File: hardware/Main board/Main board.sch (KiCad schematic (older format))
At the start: 101 parts, among them J1 Wind Direction, J10 Free Pins, J11 Nokia 5110 LCD, J2 Wind Speed, J3 USB_B_Micro, J4 Micro_SD_Card, J5 Sensor board connector, J6 Barrel_Jack, J7 ISP programmer, J8 SPI1, J9 SPI2, Q1 IRLML2060, SW1 SW_Push, SW2 SW_SPST, SW3 SW_Push, SW4 SW_Push, SW5 Page Switch btn, U1 FT232RL, U2 MCP6042, U3 SCWN03A-03, U4 ATmega1284P-AU, U5 DS3231MZ, U6 ENC28J60, U7 USB6B1, U8 DRV5053, Y1 16MHZ

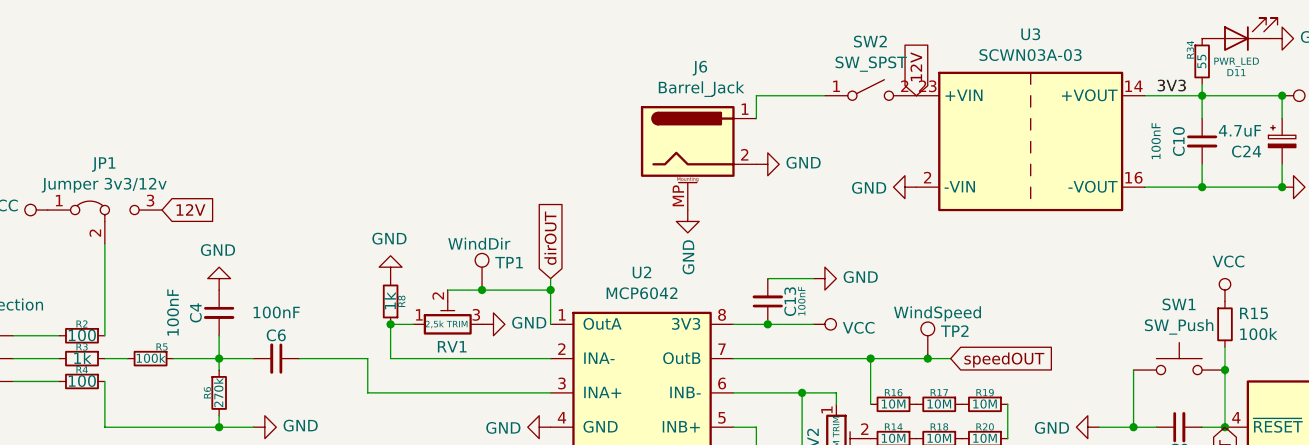
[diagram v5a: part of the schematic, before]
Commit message: Added protection for power input
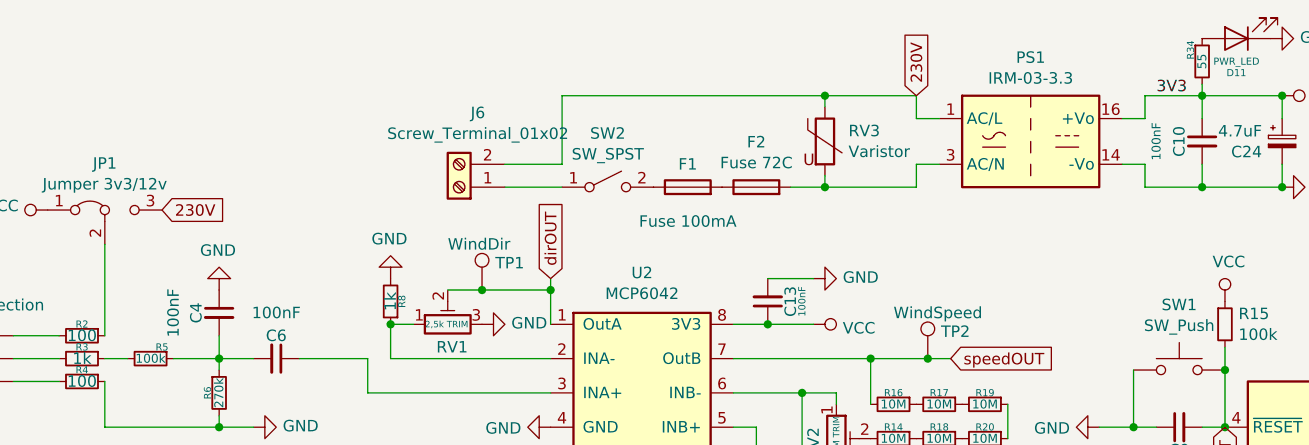
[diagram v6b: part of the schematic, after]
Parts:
- removed J6: Barrel_Jack, Connector_BarrelJack:BarrelJack_Horizontal, symbol Connector:Barrel_Jack_MountingPin
- removed U3: SCWN03A-03, Meteo_Footprints:SCWN03A, symbol Main-board-rescue:SCWN03A-03-Meteo_Station
- added F1: Fuse 100mA, Fuse:Fuseholder_Cylinder-5x20mm_Schurter_0031_8201_Horizontal_Open, symbol Device:Fuse
- added F2: Fuse 72C, Meteo_Footprints:Thermal fuse, symbol Device:Fuse
- added J6: Screw_Terminal_01x02, TerminalBlock_RND:TerminalBlock_RND_205-00298_1x02_P10.00mm_Horizontal, symbol Connector:Screw_Terminal_01x02
- added PS1: IRM-03-3.3, Converter_ACDC:Converter_ACDC_MeanWell_IRM-03-xx_THT, symbol Converter_ACDC:IRM-03-12
- added RV3: Varistor, Capacitor_SMD:C_0603_1608Metric_Pad1.05x0.95mm_HandSolder, symbol Device:Varistor
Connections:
- net GND: now also PS1.14 (-Vo)
- net VCC: now also PS1.16 (+Vo)
- net at SW2.1 (A): now also J6.1 (Pin_1)
- net 12V: no longer names the net of SW2.2 (B)
- net 12V: now also F1.1; no longer JP1.3 (B)
- new net: F1.2, F2.1
- new net: F2.2, PS1.3 (AC/N), RV3.2
- new net 230V: J6.2 (Pin_2), JP1.3 (B), PS1.1 (AC/L), RV3.1
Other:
- moved on the sheet: SW2
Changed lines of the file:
@@
 Wire Wire Line
 	2650 3450 3300 3450
-$Comp
-L Main-board-rescue:SCWN03A-03-Meteo_Station U3
-U 1 1 5D3F6E91
-P 5500 1000
-F 0 "U3" H 5500 1467 50  0000 C CNN
-F 1 "SCWN03A-03" H 5500 1376 50  0000 C CNN
-F 2 "Meteo_Footprints:SCWN03A" H 5500 650 50  0001 C CIN
-F 3 "" H 5500 550 50  0001 C CNN
-	1    5500 1000
-	1    0    0    -1
-$EndComp
 Wire Wire Line
 	6000 800  6250 800
@@
 NoConn ~ 9900 900
 $Comp
-L Connector:Barrel_Jack_MountingPin J6
-U 1 1 5D473214
-P 4000 1000
-F 0 "J6" H 4057 1325 50  0000 C CNN
-F 1 "Barrel_Jack" H 4057 1234 50  0000 C CNN
-F 2 "Connector_BarrelJack:BarrelJack_Horizontal" H 4050 960 50  0001 C CNN
-F 3 "~" H 4050 960 50  0001 C CNN
-	1    4000 1000
-	1    0    0    -1
-$EndComp
-$Comp
 L Device:R_Small R21
 U 1 1 5D4A50CE
@@
 L Switch:SW_SPST SW2
 U 1 1 5D4E4AA2
-P 4800 800
-F 0 "SW2" H 4800 1035 50  0000 C CNN
-F 1 "SW_SPST" H 4800 944 50  0000 C CNN
-F 2 "Meteo footprint:Switch_ON_OFF" H 4800 800 50  0001 C CNN
-F 3 "~" H 4800 800 50  0001 C CNN
-	1    4800 800
-	1    0    0    -1
-$EndComp
-Wire Wire Line
-	4300 900  4300 800
-Wire Wire Line
-	4300 800  4600 800
+P 3650 1200
+F 0 "SW2" H 3650 1435 50  0000 C CNN
+F 1 "SW_SPST" H 3650 1344 50  0000 C CNN
+F 2 "Meteo footprint:Switch_ON_OFF" H 3650 1200 50  0001 C CNN
+F 3 "~" H 3650 1200 50  0001 C CNN
+	1    3650 1200
+	1    0    0    -1
+$EndComp
 $Comp
 L Power_Protection:USB6B1 U7
@@
 $EndComp
 Text GLabel 5000 800  1    50   Input ~ 0
-12V
+230V
 Text GLabel 1700 1300 2    50   Input ~ 0
-12V
+230V
 Wire Wire Line
 	1450 1450 1450 1850
@@
 	6250 800  6250 750
 $Comp
-L power:GND #PWR0118
-U 1 1 5D3AC36E
-P 4000 1300
-F 0 "#PWR0118" H 4000 1050 50  0001 C CNN
-F 1 "GND" V 4005 1172 50  0000 R CNN
-F 2 "" H 4000 1300 50  0001 C CNN
-F 3 "" H 4000 1300 50  0001 C CNN
-	1    4000 1300
-	1    0    0    -1
-$EndComp
-$Comp
 L power:GND #PWR0119
 U 1 1 5D3AC7E0
@@
 $EndComp
 $Comp
-L power:GND #PWR0110
-U 1 1 5D3ED775
-P 4300 1100
-F 0 "#PWR0110" H 4300 850 50  0001 C CNN
-F 1 "GND" V 4305 972 50  0000 R CNN
-F 2 "" H 4300 1100 50  0001 C CNN
-F 3 "" H 4300 1100 50  0001 C CNN
-	1    4300 1100
-	0    -1   -1   0
-$EndComp
-$Comp
-L power:GND #PWR0122
-U 1 1 5D3EDB11
-P 5000 1200
-F 0 "#PWR0122" H 5000 950 50  0001 C CNN
-F 1 "GND" V 5005 1072 50  0000 R CNN
-F 2 "" H 5000 1200 50  0001 C CNN
-F 3 "" H 5000 1200 50  0001 C CNN
-	1    5000 1200
-	0    1    1    0
-$EndComp
-$Comp
 L Device:CP_Small C24
 U 1 1 5D3EE908
@@
 	6250 1200 6600 1200
 Connection ~ 6600 1200
+$Comp
+L Device:Fuse F1
+U 1 1 5D3F731C
+P 4000 1200
+F 0 "F1" V 4100 1200 50  0000 C CNN
+F 1 "Fuse 100mA" V 3850 1200 50  0000 C CNN
+F 2 "Fuse:Fuseholder_Cylinder-5x20mm_Schurter_0031_8201_Horizontal_Open" V 3930 1200 50  0001 C CNN
+F 3 "~" H 4000 1200 50  0001 C CNN
+	1    4000 1200
+	0    -1   -1   0
+$EndComp
+$Comp
+L Connector:Screw_Terminal_01x02 J6
+U 1 1 5D404986
+P 3000 1200
+F 0 "J6" H 2918 875 50  0000 C CNN
+F 1 "Screw_Terminal_01x02" H 2918 966 50  0000 C CNN
+F 2 "TerminalBlock_RND:TerminalBlock_RND_205-00298_1x02_P10.00mm_Horizontal" H 3000 1200 50  0001 C CNN
+F 3 "~" H 3000 1200 50  0001 C CNN
+	1    3000 1200
+	-1   0    0    1
+$EndComp
+$Comp
+L Device:Varistor RV3
+U 1 1 5D406864
+P 4600 1000
+F 0 "RV3" H 4703 1046 50  0000 L CNN
+F 1 "Varistor" H 4703 955 50  0000 L CNN
+F 2 "Capacitor_SMD:C_0603_1608Metric_Pad1.05x0.95mm_HandSolder" V 4530 1000 50  0001 C CNN
+F 3 "~" H 4600 1000 50  0001 C CNN
+	1    4600 1000
+	1    0    0    -1
+$EndComp
+$Comp
+L Device:Fuse F2
+U 1 1 5D409E09
+P 4300 1200
+F 0 "F2" V 4497 1200 50  0000 C CNN
+F 1 "Fuse 72C" V 4406 1200 50  0000 C CNN
+F 2 "Meteo_Footprints:Thermal fuse" V 4230 1200 50  0001 C CNN
+F 3 "~" H 4300 1200 50  0001 C CNN
+	1    4300 1200
+	0    -1   -1   0
+$EndComp
+Wire Wire Line
+	4600 800  4600 850
+Wire Wire Line
+	4600 1150 4600 1200
+Wire Wire Line
+	4600 1200 5000 1200
+Connection ~ 4600 1200
+Wire Wire Line
+	4450 1200 4600 1200
+Wire Wire Line
+	3200 1200 3450 1200
+$Comp
+L Converter_ACDC:IRM-03-12 PS1
+U 1 1 5D474BC1
+P 5500 1000
+F 0 "PS1" H 5500 1367 50  0000 C CNN
+F 1 "IRM-03-3.3" H 5500 1276 50  0000 C CNN
+F 2 "Converter_ACDC:Converter_ACDC_MeanWell_IRM-03-xx_THT" H 5500 650 50  0001 C CNN
+F 3 "https://www.meanwell.com/Upload/PDF/IRM-03/IRM-03-SPEC.PDF" H 5500 600 50  0001 C CNN
+	1    5500 1000
+	1    0    0    -1
+$EndComp
+Wire Wire Line
+	3200 1100 3450 1100
+Wire Wire Line
+	3450 1100 3450 800
+Wire Wire Line
+	3450 800  4600 800
+Wire Wire Line
+	4600 800  5000 800
+Wire Wire Line
+	5000 800  5000 900
+Wire Wire Line
+	5000 900  5100 900
+Connection ~ 4600 800
+Wire Wire Line
+	5000 1200 5000 1100
+Wire Wire Line
+	5000 1100 5100 1100
+Wire Wire Line
+	5900 900  6000 900
+Wire Wire Line
+	6000 900  6000 800
+Wire Wire Line
+	5900 1100 6000 1100
+Wire Wire Line
+	6000 1100 6000 1200
 $EndSCHEMATC

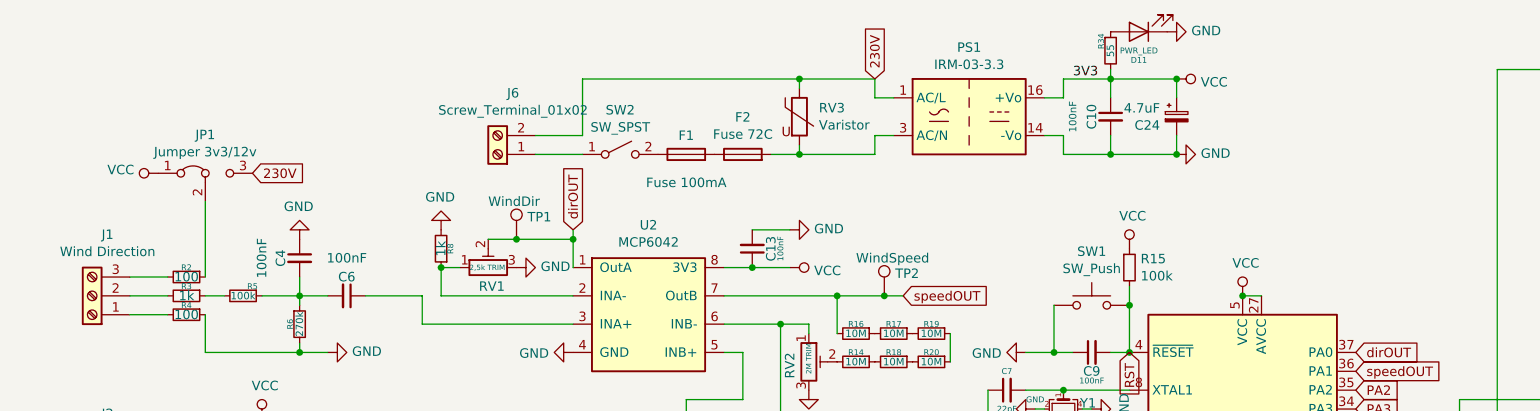
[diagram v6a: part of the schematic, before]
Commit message: Updated the power supply input
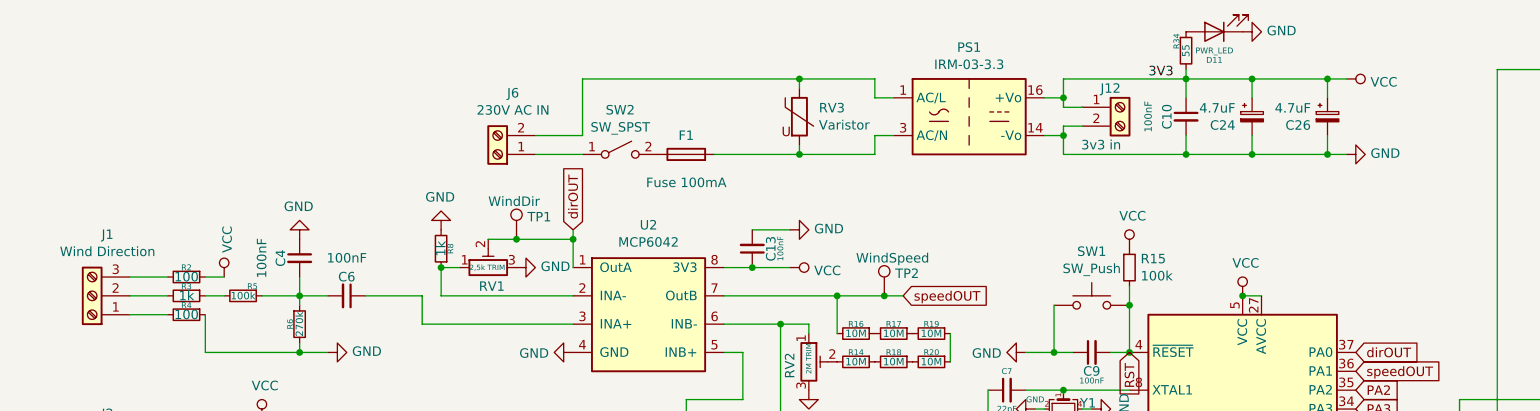
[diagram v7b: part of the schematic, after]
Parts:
- removed F2: Fuse 72C, Meteo_Footprints:Thermal fuse, symbol Device:Fuse
- removed JP1: Jumper 3v3/12v, Connector_PinHeader_2.54mm:PinHeader_1x03_P2.54mm_Vertical, symbol Jumper:Jumper_3_Bridged12
- added C26: 4.7uF, Capacitor_SMD:CP_Elec_4x5.4, symbol Device:CP_Small
- added J12: 3v3 in, TerminalBlock:TerminalBlock_Altech_AK300-2_P5.00mm, symbol Connector:Screw_Terminal_01x02
- J6: value Screw_Terminal_01x02 -> 230V AC IN
- SW2: footprint Meteo footprint:Switch_ON_OFF -> Meteo_Footprints:Switch_NEW
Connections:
- net GND: now also C26.2, J12.2 (Pin_2)
- net VCC: now also R2.1, C26.1, J12.1 (Pin_1)
- net at F1.2: now also PS1.3 (AC/N), RV3.2
- net 230V: no longer names the net of J6.2 (Pin_2), PS1.1 (AC/L), RV3.1
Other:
- moved on the sheet: C10, C24, D11, R34
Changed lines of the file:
@@
 L Device:C_Small C10
 U 1 1 5D31C05B
-P 6250 1000
-F 0 "C10" V 6150 1000 50  0000 C CNN
-F 1 "100nF" V 6050 1000 39  0000 C CNN
-F 2 "Capacitor_SMD:C_0805_2012Metric_Pad1.15x1.40mm_HandSolder" H 6250 1000 50  0001 C CNN
-F 3 "~" H 6250 1000 50  0001 C CNN
-	1    6250 1000
+P 6650 1000
+F 0 "C10" V 6550 1000 50  0000 C CNN
+F 1 "100nF" V 6450 1000 39  0000 C CNN
+F 2 "Capacitor_SMD:C_0805_2012Metric_Pad1.15x1.40mm_HandSolder" H 6650 1000 50  0001 C CNN
+F 3 "~" H 6650 1000 50  0001 C CNN
+	1    6650 1000
 	1    0    0    -1
 $EndComp
@@
 	2650 3450 3300 3450
 Wire Wire Line
-	6000 800  6250 800
-Wire Wire Line
-	6250 900  6250 800
-Wire Wire Line
-	6000 1200 6250 1200
-Connection ~ 6250 800
-Wire Wire Line
-	6250 1100 6250 1200
-Connection ~ 6250 1200
-Text Label 6050 800  0    50   ~ 0
+	6650 900  6650 800
+Connection ~ 6650 800
+Wire Wire Line
+	6650 1100 6650 1200
+Connection ~ 6650 1200
+Text Label 6450 800  0    50   ~ 0
 3V3
 Wire Wire Line
@@
 F 0 "SW2" H 3650 1435 50  0000 C CNN
 F 1 "SW_SPST" H 3650 1344 50  0000 C CNN
-F 2 "Meteo footprint:Switch_ON_OFF" H 3650 1200 50  0001 C CNN
+F 2 "Meteo_Footprints:Switch_NEW" H 3650 1200 50  0001 C CNN
 F 3 "~" H 3650 1200 50  0001 C CNN
 	1    3650 1200
@@
 L power:GND #PWR031
 U 1 1 5D3744FF
-P 6600 1200
-F 0 "#PWR031" H 6600 950 50  0001 C CNN
-F 1 "GND" V 6605 1072 50  0000 R CNN
-F 2 "" H 6600 1200 50  0001 C CNN
-F 3 "" H 6600 1200 50  0001 C CNN
-	1    6600 1200
+P 7500 1200
+F 0 "#PWR031" H 7500 950 50  0001 C CNN
+F 1 "GND" V 7505 1072 50  0000 R CNN
+F 2 "" H 7500 1200 50  0001 C CNN
+F 3 "" H 7500 1200 50  0001 C CNN
+	1    7500 1200
 	0    -1   -1   0
 $EndComp
@@
 L power:VCC #PWR030
 U 1 1 5D377A4D
-P 6600 800
-F 0 "#PWR030" H 6600 650 50  0001 C CNN
-F 1 "VCC" V 6617 928 50  0000 L CNN
-F 2 "" H 6600 800 50  0001 C CNN
-F 3 "" H 6600 800 50  0001 C CNN
-	1    6600 800
+P 7500 800
+F 0 "#PWR030" H 7500 650 50  0001 C CNN
+F 1 "VCC" V 7517 928 50  0000 L CNN
+F 2 "" H 7500 800 50  0001 C CNN
+F 3 "" H 7500 800 50  0001 C CNN
+	1    7500 800
 	0    1    1    0
 $EndComp
@@
 $EndComp
 $Comp
-L power:VCC #PWR04
-U 1 1 5D382ED3
-P 1200 1300
-F 0 "#PWR04" H 1200 1150 50  0001 C CNN
-F 1 "VCC" V 1218 1427 50  0000 L CNN
-F 2 "" H 1200 1300 50  0001 C CNN
-F 3 "" H 1200 1300 50  0001 C CNN
-	1    1200 1300
-	0    -1   -1   0
-$EndComp
-$Comp
 L power:VCC #PWR07
 U 1 1 5D383503
@@
 	1    0    0    -1
 $EndComp
-$Comp
-L Jumper:Jumper_3_Bridged12 JP1
-U 1 1 5D38903C
-P 1450 1300
-F 0 "JP1" H 1450 1504 50  0000 C CNN
-F 1 "Jumper 3v3/12v" H 1450 1413 50  0000 C CNN
-F 2 "Connector_PinHeader_2.54mm:PinHeader_1x03_P2.54mm_Vertical" H 1450 1300 50  0001 C CNN
-F 3 "~" H 1450 1300 50  0001 C CNN
-	1    1450 1300
-	1    0    0    -1
-$EndComp
-Text GLabel 5000 800  1    50   Input ~ 0
-230V
-Text GLabel 1700 1300 2    50   Input ~ 0
-230V
-Wire Wire Line
-	1450 1450 1450 1850
 Wire Wire Line
 	4500 2100 4650 2100
@@
 L Device:LED D11
 U 1 1 5D5D908D
-P 6400 550
-F 0 "D11" H 6400 700 31  0000 C CNN
-F 1 "PWR_LED" H 6400 650 31  0000 C CNN
-F 2 "Diode_SMD:D_0805_2012Metric" H 6400 550 50  0001 C CNN
-F 3 "~" H 6400 550 50  0001 C CNN
-	1    6400 550
+P 6800 550
+F 0 "D11" H 6800 700 31  0000 C CNN
+F 1 "PWR_LED" H 6800 650 31  0000 C CNN
+F 2 "Diode_SMD:D_0805_2012Metric" H 6800 550 50  0001 C CNN
+F 3 "~" H 6800 550 50  0001 C CNN
+	1    6800 550
 	-1   0    0    1
 $EndComp
@@
 L Device:R_Small R34
 U 1 1 5D5E6FB6
-P 6250 650
-F 0 "R34" V 6200 700 31  0000 C CNN
-F 1 "55" V 6250 650 39  0000 C CNN
-F 2 "Resistor_SMD:R_0805_2012Metric" H 6250 650 50  0001 C CNN
-F 3 "~" H 6250 650 50  0001 C CNN
-	1    6250 650
+P 6650 650
+F 0 "R34" V 6600 700 31  0000 C CNN
+F 1 "55" V 6650 650 39  0000 C CNN
+F 2 "Resistor_SMD:R_0805_2012Metric" H 6650 650 50  0001 C CNN
+F 3 "~" H 6650 650 50  0001 C CNN
+	1    6650 650
 	1    0    0    -1
 $EndComp
@@
 L power:GND #PWR0117
 U 1 1 5D5D94D8
-P 6550 550
-F 0 "#PWR0117" H 6550 300 50  0001 C CNN
-F 1 "GND" V 6555 422 50  0000 R CNN
-F 2 "" H 6550 550 50  0001 C CNN
-F 3 "" H 6550 550 50  0001 C CNN
-	1    6550 550
-	0    -1   -1   0
-$EndComp
-Wire Wire Line
-	6250 800  6250 750
+P 6950 550
+F 0 "#PWR0117" H 6950 300 50  0001 C CNN
+F 1 "GND" V 6955 422 50  0000 R CNN
+F 2 "" H 6950 550 50  0001 C CNN
+F 3 "" H 6950 550 50  0001 C CNN
+	1    6950 550
+	0    -1   -1   0
+$EndComp
+Wire Wire Line
+	6650 800  6650 750
 $Comp
 L power:GND #PWR0119
@@
 L Device:CP_Small C24
 U 1 1 5D3EE908
-P 6600 1000
-F 0 "C24" H 6512 954 50  0000 R CNN
-F 1 "4.7uF" H 6512 1045 50  0000 R CNN
-F 2 "Capacitor_SMD:CP_Elec_4x5.4" H 6600 1000 50  0001 C CNN
-F 3 "~" H 6600 1000 50  0001 C CNN
-	1    6600 1000
-	1    0    0    -1
-$EndComp
-Wire Wire Line
-	6600 800  6600 900
-Wire Wire Line
-	6250 800  6600 800
-Connection ~ 6600 800
-Wire Wire Line
-	6600 1200 6600 1100
-Wire Wire Line
-	6250 1200 6600 1200
-Connection ~ 6600 1200
+P 7000 1000
+F 0 "C24" H 6912 954 50  0000 R CNN
+F 1 "4.7uF" H 6912 1045 50  0000 R CNN
+F 2 "Capacitor_SMD:CP_Elec_4x5.4" H 7000 1000 50  0001 C CNN
+F 3 "~" H 7000 1000 50  0001 C CNN
+	1    7000 1000
+	1    0    0    -1
+$EndComp
+Wire Wire Line
+	7000 800  7000 900
+Wire Wire Line
+	6650 800  7000 800
+Connection ~ 7000 800
+Wire Wire Line
+	7000 1200 7000 1100
+Wire Wire Line
+	6650 1200 7000 1200
 $Comp
 L Device:Fuse F1
@@
 P 3000 1200
 F 0 "J6" H 2918 875 50  0000 C CNN
-F 1 "Screw_Terminal_01x02" H 2918 966 50  0000 C CNN
+F 1 "230V AC IN" H 2918 966 50  0000 C CNN
 F 2 "TerminalBlock_RND:TerminalBlock_RND_205-00298_1x02_P10.00mm_Horizontal" H 3000 1200 50  0001 C CNN
 F 3 "~" H 3000 1200 50  0001 C CNN
@@
 	1    0    0    -1
 $EndComp
-$Comp
-L Device:Fuse F2
-U 1 1 5D409E09
-P 4300 1200
-F 0 "F2" V 4497 1200 50  0000 C CNN
-F 1 "Fuse 72C" V 4406 1200 50  0000 C CNN
-F 2 "Meteo_Footprints:Thermal fuse" V 4230 1200 50  0001 C CNN
-F 3 "~" H 4300 1200 50  0001 C CNN
-	1    4300 1200
-	0    -1   -1   0
-$EndComp
 Wire Wire Line
 	4600 800  4600 850
@@
 	4600 1200 5000 1200
 Connection ~ 4600 1200
-Wire Wire Line
-	4450 1200 4600 1200
 Wire Wire Line
 	3200 1200 3450 1200
@@
 	5900 900  6000 900
 Wire Wire Line
+	5900 1100 6000 1100
+$Comp
+L power:VCC #PWR0110
+U 1 1 5D4223D8
+P 1550 1850
+F 0 "#PWR0110" H 1550 1700 50  0001 C CNN
+F 1 "VCC" V 1567 1978 50  0000 L CNN
+F 2 "" H 1550 1850 50  0001 C CNN
+F 3 "" H 1550 1850 50  0001 C CNN
+	1    1550 1850
+	1    0    0    -1
+$EndComp
+Wire Wire Line
+	1550 1850 1450 1850
+Wire Wire Line
+	4150 1200 4600 1200
+Wire Wire Line
+	6000 900  6000 950
+Wire Wire Line
+	6000 950  6100 950
+Wire Wire Line
+	6000 1100 6000 1050
+Wire Wire Line
+	6000 1050 6100 1050
+Wire Wire Line
+	6000 1100 6000 1200
+Wire Wire Line
+	6000 1200 6650 1200
+Connection ~ 6000 1100
+Wire Wire Line
 	6000 900  6000 800
 Wire Wire Line
-	5900 1100 6000 1100
-Wire Wire Line
-	6000 1100 6000 1200
+	6000 800  6650 800
+Connection ~ 6000 900
+$Comp
+L Connector:Screw_Terminal_01x02 J12
+U 1 1 5D48A33C
+P 6300 950
+F 0 "J12" H 6250 1050 50  0000 C CNN
+F 1 "3v3 in" H 6200 750 50  0000 C CNN
+F 2 "TerminalBlock:TerminalBlock_Altech_AK300-2_P5.00mm" H 6300 950 50  0001 C CNN
+F 3 "~" H 6300 950 50  0001 C CNN
+	1    6300 950
+	1    0    0    -1
+$EndComp
+Wire Wire Line
+	7000 800  7400 800
+Wire Wire Line
+	7000 1200 7400 1200
+Connection ~ 7000 1200
+Wire Wire Line
+	7400 1100 7400 1200
+Connection ~ 7400 1200
+Wire Wire Line
+	7400 1200 7500 1200
+Wire Wire Line
+	7400 900  7400 800
+Connection ~ 7400 800
+Wire Wire Line
+	7400 800  7500 800
+$Comp
+L Device:CP_Small C26
+U 1 1 5D5182A6
+P 7400 1000
+F 0 "C26" H 7312 954 50  0000 R CNN
+F 1 "4.7uF" H 7312 1045 50  0000 R CNN
+F 2 "Capacitor_SMD:CP_Elec_4x5.4" H 7400 1000 50  0001 C CNN
+F 3 "~" H 7400 1000 50  0001 C CNN
+	1    7400 1000
+	1    0    0    -1
+$EndComp
 $EndSCHEMATC
